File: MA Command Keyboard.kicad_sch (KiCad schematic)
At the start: 16 parts

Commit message: Placing Finished
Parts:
- C1, C2, C3, C4, C5, C6, C7: renamed from C?; footprint (none) -> Capacitor_SMD:C_0805_2012Metric
- F1: renamed from F?; footprint (none) -> Fuse:Fuse_1206_3216Metric
- R1, R2, R3, R4: renamed from R?; footprint (none) -> Resistor_SMD:R_0805_2012Metric
- SW1: renamed from SW?; footprint (none) -> random-keyboard-parts:SKQG-1155865
- USB1: renamed from USB?; footprint (none) -> random-keyboard-parts:Molex-0548190589
- Y1: renamed from Y?; footprint (none) -> Crystal:Crystal_SMD_3225-4Pin_3.2x2.5mm
- gave numbers to parts that had none: 1

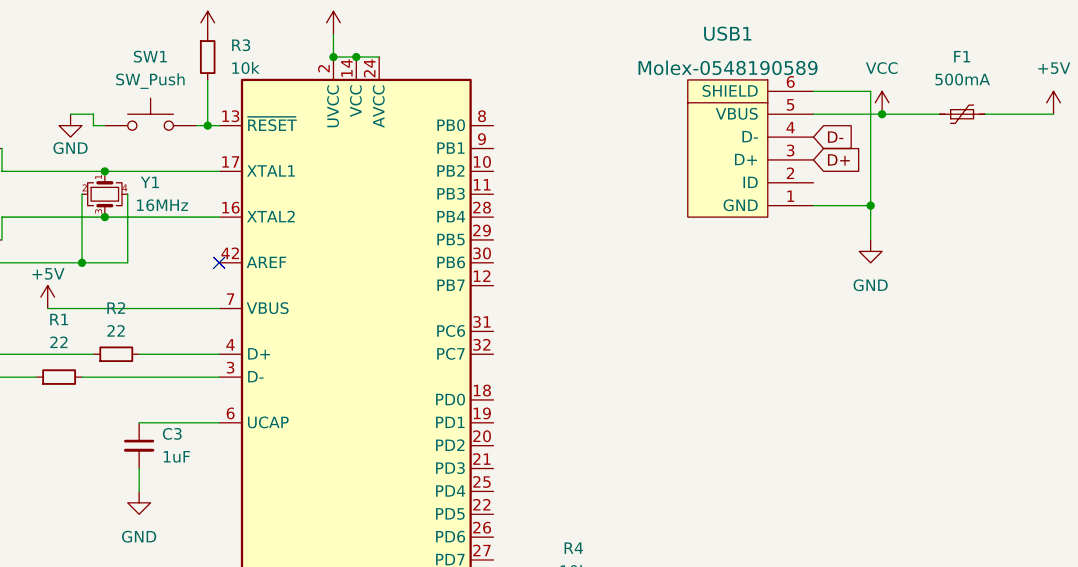
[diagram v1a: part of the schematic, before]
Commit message: Matrix Traces in
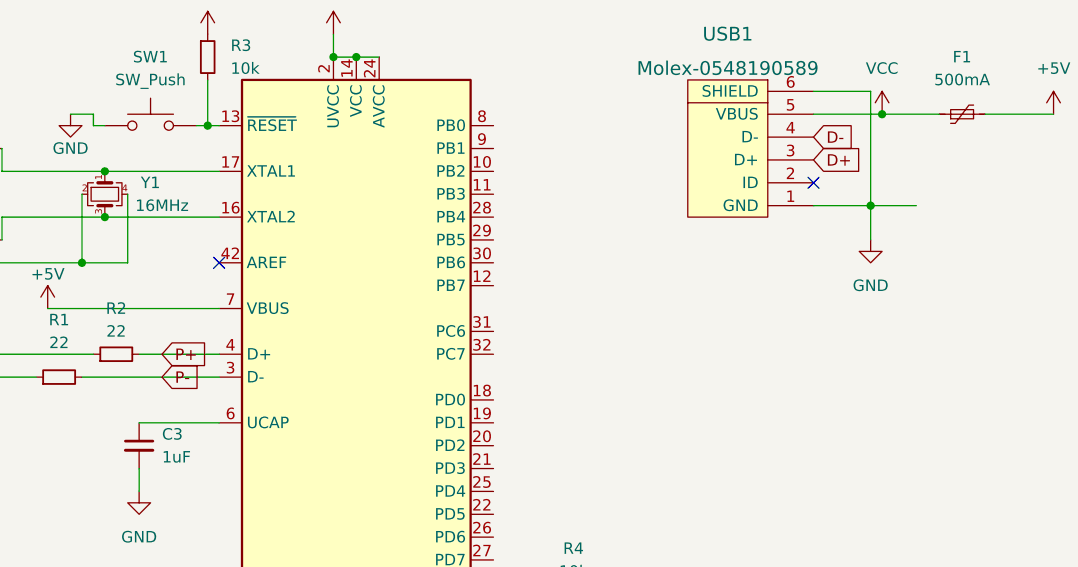
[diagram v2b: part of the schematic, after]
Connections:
- net P-: now reaches R1.2, U1.3 (D-)
- net P+: now reaches R2.2, U1.4 (D+)
- no-connect marks 1 -> 2
